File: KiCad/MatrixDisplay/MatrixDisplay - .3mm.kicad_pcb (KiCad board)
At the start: 2 copper layers, 3 parts, among them J1 PUT_IN, J2 Power, U1 mini_esp32

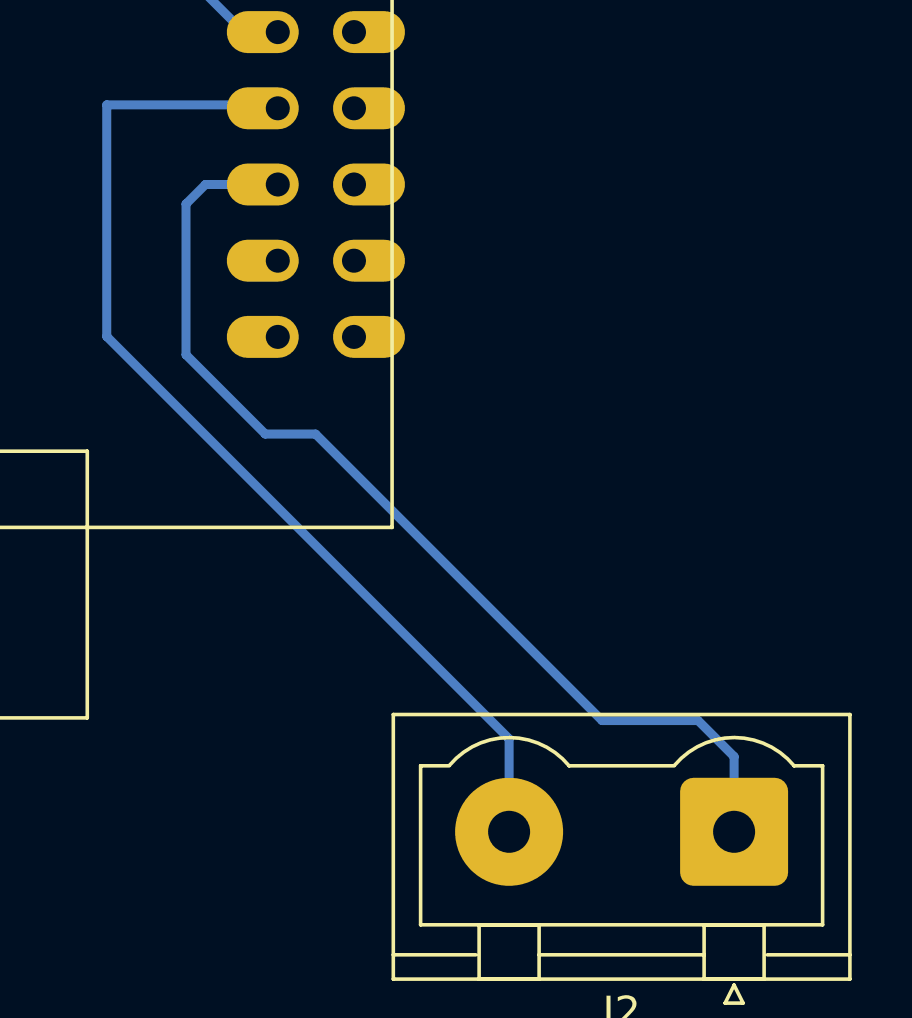
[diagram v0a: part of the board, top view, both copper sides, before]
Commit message: add wifi setup instructins to display
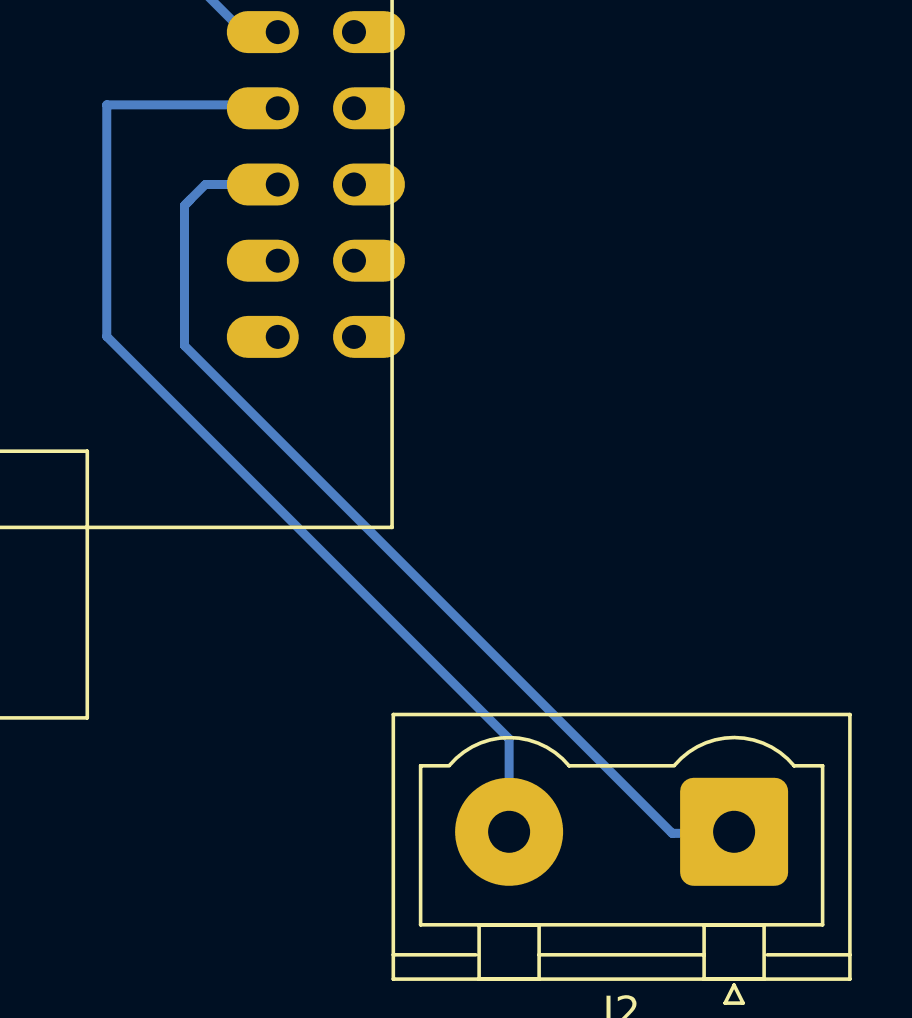
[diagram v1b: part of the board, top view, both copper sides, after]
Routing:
- net Net-(J2-Pad1): track 34.7 -> 33.3 mm
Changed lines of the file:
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@@
     (pad_to_mask_clearance 0)
     (pcbplotparams
-      (layerselection 0x0040000_7ffffffe)
+      (layerselection 0x0040000_fffffffe)
       (disableapertmacros false)
       (usegerberextensions false)
@@
     (effects (font (size 2 2) (thickness 0.15)))
   )
-  (segment (start 137.3124 125.4252) (end 135.636 125.4252) (width 0.3) (layer "B.Cu") (net 1))
-  (segment (start 150.0632 134.9756) (end 146.8628 134.9756) (width 0.3) (layer "B.Cu") (net 1))
+  (segment (start 151.264 138.684) (end 151.2316 138.684) (width 0.3) (layer "B.Cu") (net 1))
+  (segment (start 132.9436 122.4788) (end 132.9436 117.8052) (width 0.3) (layer "B.Cu") (net 1))
+  (segment (start 132.9944 117.7544) (end 133.1214 117.6274) (width 0.3) (layer "B.Cu") (net 1))
+  (segment (start 151.2316 138.684) (end 151.1808 138.7348) (width 0.3) (layer "B.Cu") (net 1))
   (segment (start 133.6418 117.107) (end 136.053 117.107) (width 0.3) (layer "B.Cu") (net 1))
-  (segment (start 146.8628 134.9756) (end 137.3124 125.4252) (width 0.3) (layer "B.Cu") (net 1))
-  (segment (start 132.9944 117.7544) (end 133.6418 117.107) (width 0.3) (layer "B.Cu") (net 1))
-  (segment (start 151.264 136.1764) (end 150.0632 134.9756) (width 0.3) (layer "B.Cu") (net 1))
-  (segment (start 151.264 138.684) (end 151.264 136.1764) (width 0.3) (layer "B.Cu") (net 1))
-  (segment (start 132.9944 122.7836) (end 132.9944 117.7544) (width 0.3) (layer "B.Cu") (net 1))
-  (segment (start 135.636 125.4252) (end 132.9944 122.7836) (width 0.3) (layer "B.Cu") (net 1))
+  (segment (start 149.1996 138.7348) (end 132.9436 122.4788) (width 0.3) (layer "B.Cu") (net 1))
+  (segment (start 132.9436 117.8052) (end 133.1214 117.6274) (width 0.3) (layer "B.Cu") (net 1))
+  (segment (start 151.1808 138.7348) (end 149.1996 138.7348) (width 0.3) (layer "B.Cu") (net 1))
+  (segment (start 133.1214 117.6274) (end 133.6418 117.107) (width 0.3) (layer "B.Cu") (net 1))
   (segment (start 140.99252 101.37428) (end 140.4998 101.867) (width 0.3) (layer "B.Cu") (net 2))
   (segment (start 140.4998 101.867) (end 138.593 101.867) (width 0.3) (layer "B.Cu") (net 2))
